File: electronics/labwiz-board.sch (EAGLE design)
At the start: 99 parts, among them J1 SD_MICRO_SDIO_1BIT, J2 CORTEX_DEBUGSMD_original, J3 DNP, U1 STM32F10XRXT6, U2 MCP73831/2, U4 MIC5219-3.3V, X2 M12_BOTTOM_CONTACTS_FPC_1MM, Y3 32.768kHz

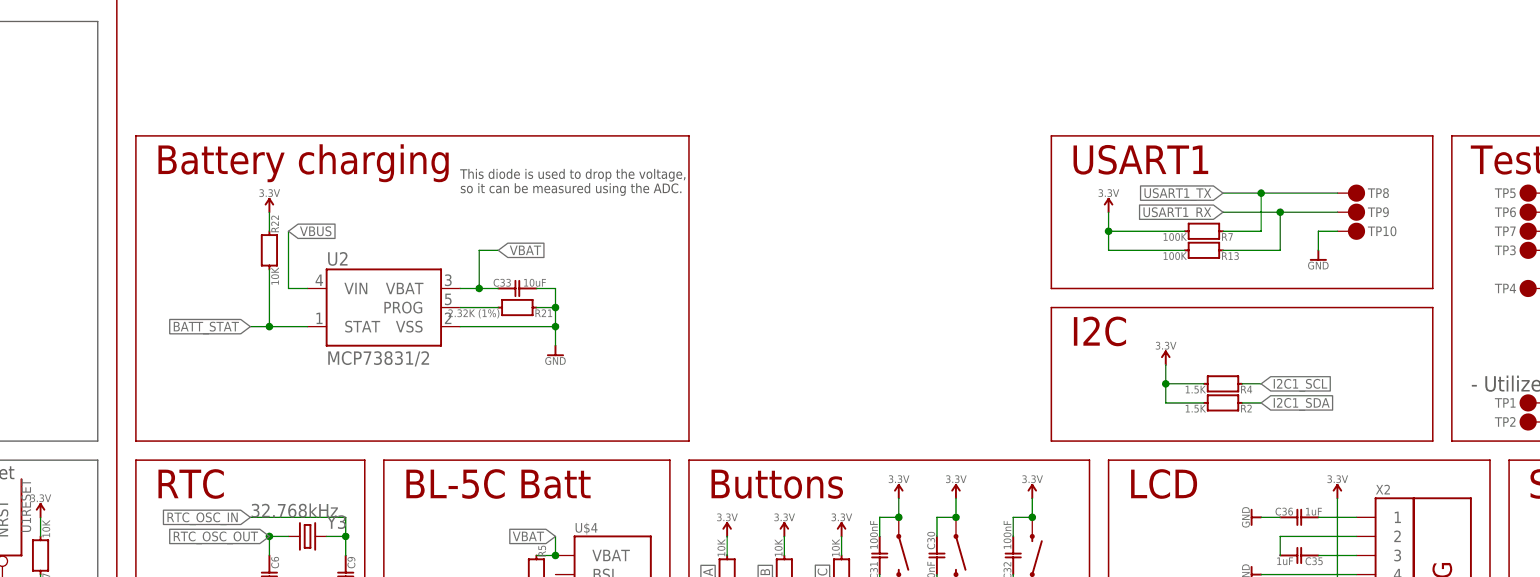
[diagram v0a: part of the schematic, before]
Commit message: Added 2x2 right angle header to board. Closes #105.
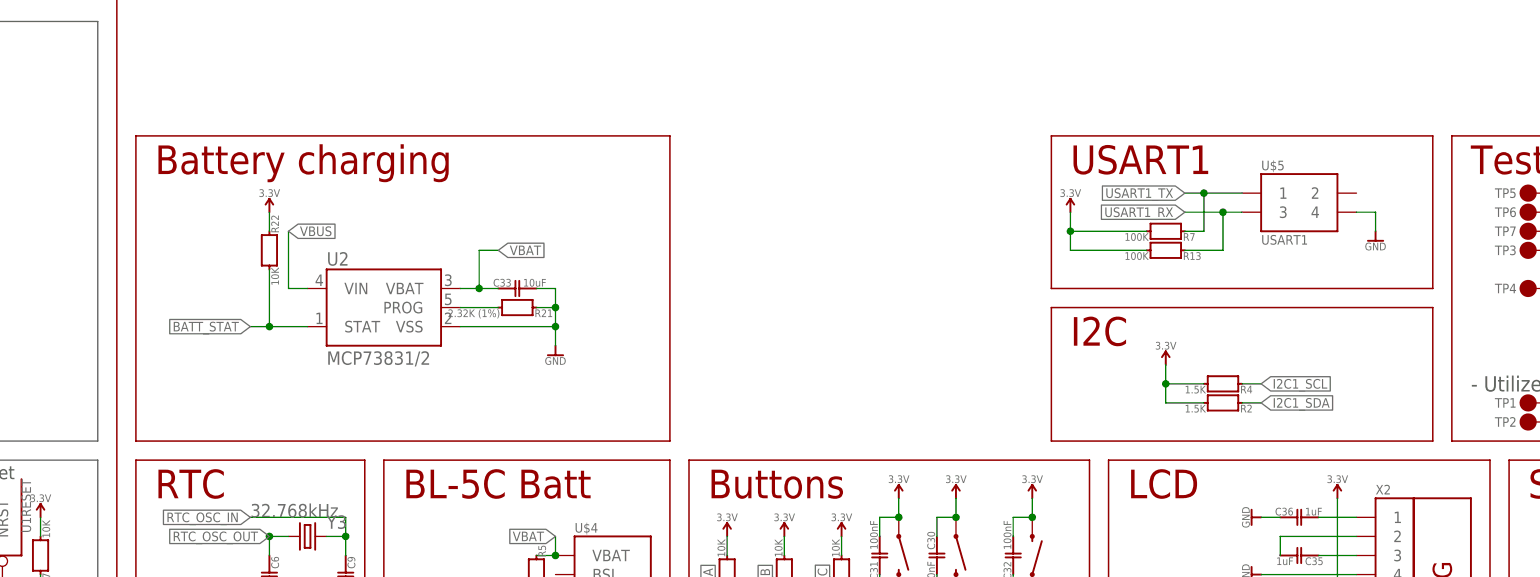
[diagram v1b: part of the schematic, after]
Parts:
- removed TP10, TP8, TP9: DNP, PaxInstruments-Connectors:M01_PAD_1MM
- added U$5: USART1, PaxInstruments-Connectors:M02X2_RIGHT_ANGLE
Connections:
- net GND: now also U$5.4; no longer TP10.P$1
- net USART1_RX: now also U$5.3; no longer TP9.P$1
- net USART1_TX: now also U$5.1; no longer TP8.P$1
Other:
- note removed: "This diode is used to drop the voltage, so it can be measured using the ADC."
- moved on the sheet: R13, R7
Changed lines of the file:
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@@
 <part name="TP7" library="PaxInstruments-Connectors" deviceset="M01" device="_PAD_1MM" value="DNP"/>
 <part name="GND21" library="PaxInstruments-Aesthetics" deviceset="GND" device="" value="GND"/>
-<part name="TP8" library="PaxInstruments-Connectors" deviceset="M01" device="_PAD_1MM" value="DNP"/>
-<part name="TP9" library="PaxInstruments-Connectors" deviceset="M01" device="_PAD_1MM" value="DNP"/>
-<part name="TP10" library="PaxInstruments-Connectors" deviceset="M01" device="_PAD_1MM" value="DNP"/>
 <part name="F1" library="PaxInstruments-RCL" deviceset="FUSE_RESETTABLE_PTC" device="_0805" technology="_1000MA" value="1000mA"/>
 <part name="Z3" library="PaxInstrument-T400" deviceset="SPARKFUN-RESISTORS_RESISTOR" device="0603-RES" value="PGB1010603">
@@
 <part name="C17" library="PaxInstruments-RCL" deviceset="CAPACITOR_FIXED" device="_0402" technology="_1UF" value="1uF"/>
 <part name="JP2" library="SparkFun-Jumpers" deviceset="JUMPER-SMT_3_1-NC_TRACE" device="_SILK"/>
+<part name="U$5" library="PaxInstruments-Connectors" deviceset="M02X2" device="_RIGHT_ANGLE" value="USART1"/>
 </parts>
 <sheets>
@@
 <wire x1="114.3" y1="5.08" x2="162.56" y2="5.08" width="0.2032" layer="94"/>
 <text x="116.84" y="40.64" size="3.81" layer="94">WiFi Module</text>
-<wire x1="187.96" y1="91.44" x2="187.96" y2="132.08" width="0.2032" layer="94"/>
-<wire x1="114.3" y1="132.08" x2="187.96" y2="132.08" width="0.2032" layer="94"/>
-<wire x1="114.3" y1="91.44" x2="187.96" y2="91.44" width="0.2032" layer="94"/>
+<wire x1="185.42" y1="91.44" x2="185.42" y2="132.08" width="0.2032" layer="94"/>
+<wire x1="114.3" y1="132.08" x2="185.42" y2="132.08" width="0.2032" layer="94"/>
+<wire x1="114.3" y1="91.44" x2="185.42" y2="91.44" width="0.2032" layer="94"/>
 <wire x1="114.3" y1="91.44" x2="114.3" y2="132.08" width="0.2032" layer="94"/>
 <text x="116.84" y="127" size="3.81" layer="94">Battery charging</text>
@@
 <wire x1="314.96" y1="198.12" x2="383.54" y2="198.12" width="0.2032" layer="94"/>
 <wire x1="383.54" y1="198.12" x2="383.54" y2="256.54" width="0.2032" layer="94"/>
-<text x="157.48" y="124.46" size="1.27" layer="97">This diode is used to drop the voltage,
-so it can be measured using the ADC.</text>
 <text x="93.98" y="185.42" size="1.27" layer="97">Shotkey diode</text>
 <text x="292.1" y="99.06" size="2.032" layer="97" align="center-left">- Utilize unused pins</text>
@@
 <instance part="C16" gate="G$1" x="165.1" y="63.5" rot="MR180"/>
 <instance part="TP7" gate="G$1" x="299.72" y="119.38" rot="R180"/>
-<instance part="GND21" gate="G$1" x="271.78" y="116.84"/>
-<instance part="TP8" gate="G$1" x="276.86" y="124.46"/>
-<instance part="TP9" gate="G$1" x="276.86" y="121.92"/>
-<instance part="TP10" gate="G$1" x="276.86" y="119.38"/>
+<instance part="GND21" gate="G$1" x="279.4" y="119.38"/>
 <instance part="F1" gate="G$1" x="45.72" y="185.42" rot="MR270"/>
 <instance part="Z3" gate="G$1" x="38.1" y="167.64" smashed="yes" rot="R90">
@@
 <attribute name="MF" x="38.1" y="167.64" size="1.778" layer="96" rot="R90" display="off"/>
 </instance>
-<instance part="R7" gate="G$1" x="256.54" y="119.38" rot="R90"/>
-<instance part="R13" gate="G$1" x="256.54" y="116.84" rot="R90"/>
-<instance part="SUPPLY5" gate="G$1" x="243.84" y="121.92"/>
+<instance part="R7" gate="G$1" x="251.46" y="119.38" rot="R90"/>
+<instance part="R13" gate="G$1" x="251.46" y="116.84" rot="R90"/>
+<instance part="SUPPLY5" gate="G$1" x="238.76" y="121.92"/>
 <instance part="C17" gate="G$1" x="83.82" y="66.04"/>
 <instance part="JP2" gate="G$1" x="53.34" y="170.18" smashed="yes" rot="MR0">
 <attribute name="NAME" x="58.42" y="173.101" size="1.778" layer="95" font="vector" rot="MR0"/>
 </instance>
+<instance part="U$5" gate="G$1" x="269.24" y="121.92"/>
 </instances>
 <busses>
@@
 <pinref part="R13" gate="G$1" pin="1"/>
 <pinref part="SUPPLY5" gate="G$1" pin="3.3V"/>
-<wire x1="254" y1="116.84" x2="243.84" y2="116.84" width="0.1524" layer="91"/>
-<wire x1="243.84" y1="116.84" x2="243.84" y2="119.38" width="0.1524" layer="91"/>
+<wire x1="248.92" y1="116.84" x2="238.76" y2="116.84" width="0.1524" layer="91"/>
+<wire x1="238.76" y1="116.84" x2="238.76" y2="119.38" width="0.1524" layer="91"/>
 <pinref part="R7" gate="G$1" pin="1"/>
-<wire x1="243.84" y1="119.38" x2="243.84" y2="121.92" width="0.1524" layer="91"/>
-<wire x1="254" y1="119.38" x2="243.84" y2="119.38" width="0.1524" layer="91"/>
-<junction x="243.84" y="119.38"/>
+<wire x1="238.76" y1="119.38" x2="238.76" y2="121.92" width="0.1524" layer="91"/>
+<wire x1="248.92" y1="119.38" x2="238.76" y2="119.38" width="0.1524" layer="91"/>
+<junction x="238.76" y="119.38"/>
 </segment>
 <segment>
@@
 </segment>
 <segment>
-<pinref part="GND21" gate="G$1" pin="GND"/>
-<wire x1="274.32" y1="119.38" x2="271.78" y2="119.38" width="0.1524" layer="91"/>
-<wire x1="271.78" y1="119.38" x2="271.78" y2="116.84" width="0.1524" layer="91"/>
-<pinref part="TP10" gate="G$1" pin="P$1"/>
-</segment>
-<segment>
 <pinref part="R16" gate="G$1" pin="1"/>
 <pinref part="GND33" gate="G$1" pin="GND"/>
 <wire x1="223.52" y1="60.96" x2="223.52" y2="53.34" width="0.1524" layer="91"/>
+</segment>
+<segment>
+<pinref part="U$5" gate="G$1" pin="4"/>
+<pinref part="GND21" gate="G$1" pin="GND"/>
+<wire x1="276.86" y1="121.92" x2="279.4" y2="121.92" width="0.1524" layer="91"/>
+<wire x1="279.4" y1="121.92" x2="279.4" y2="119.38" width="0.1524" layer="91"/>
 </segment>
 </net>
@@
 </segment>
 <segment>
-<label x="259.08" y="124.46" size="1.27" layer="95" rot="R180" xref="yes"/>
-<wire x1="259.08" y1="124.46" x2="264.16" y2="124.46" width="0.1524" layer="91"/>
-<pinref part="TP8" gate="G$1" pin="P$1"/>
+<label x="254" y="124.46" size="1.27" layer="95" rot="R180" xref="yes"/>
+<wire x1="254" y1="124.46" x2="256.54" y2="124.46" width="0.1524" layer="91"/>
 <pinref part="R7" gate="G$1" pin="2"/>
-<wire x1="264.16" y1="124.46" x2="274.32" y2="124.46" width="0.1524" layer="91"/>
-<wire x1="259.08" y1="119.38" x2="264.16" y2="119.38" width="0.1524" layer="91"/>
-<wire x1="264.16" y1="119.38" x2="264.16" y2="124.46" width="0.1524" layer="91"/>
-<junction x="264.16" y="124.46"/>
+<wire x1="254" y1="119.38" x2="256.54" y2="119.38" width="0.1524" layer="91"/>
+<wire x1="256.54" y1="119.38" x2="256.54" y2="124.46" width="0.1524" layer="91"/>
+<junction x="256.54" y="124.46"/>
+<pinref part="U$5" gate="G$1" pin="1"/>
+<wire x1="256.54" y1="124.46" x2="261.62" y2="124.46" width="0.1524" layer="91"/>
 </segment>
 <segment>
@@
 </segment>
 <segment>
-<label x="259.08" y="121.92" size="1.27" layer="95" rot="R180" xref="yes"/>
-<wire x1="259.08" y1="121.92" x2="266.7" y2="121.92" width="0.1524" layer="91"/>
-<pinref part="TP9" gate="G$1" pin="P$1"/>
+<label x="254" y="121.92" size="1.27" layer="95" rot="R180" xref="yes"/>
+<wire x1="254" y1="121.92" x2="259.08" y2="121.92" width="0.1524" layer="91"/>
 <pinref part="R13" gate="G$1" pin="2"/>
-<wire x1="266.7" y1="121.92" x2="274.32" y2="121.92" width="0.1524" layer="91"/>
-<wire x1="259.08" y1="116.84" x2="266.7" y2="116.84" width="0.1524" layer="91"/>
-<wire x1="266.7" y1="116.84" x2="266.7" y2="121.92" width="0.1524" layer="91"/>
-<junction x="266.7" y="121.92"/>
-</segment>
-<segment>
+<wire x1="254" y1="116.84" x2="259.08" y2="116.84" width="0.1524" layer="91"/>
+<wire x1="259.08" y1="116.84" x2="259.08" y2="121.92" width="0.1524" layer="91"/>
+<junction x="259.08" y="121.92"/>
+<pinref part="U$5" gate="G$1" pin="3"/>
+<wire x1="259.08" y1="121.92" x2="261.62" y2="121.92" width="0.1524" layer="91"/>
+</segment>
+<segment>

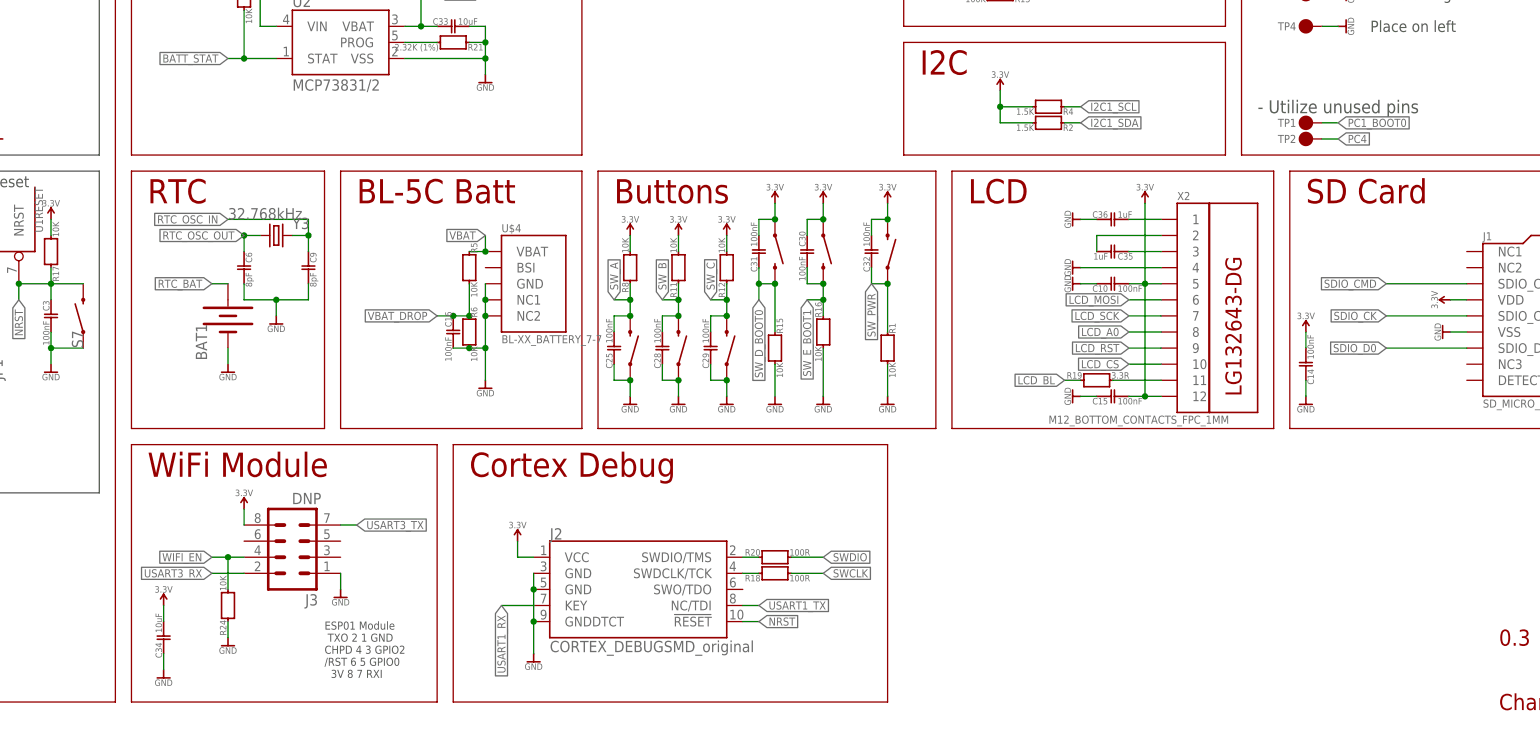
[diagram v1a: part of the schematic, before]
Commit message: Moved to ESP-09 WiFi modules. Still some work to be done.
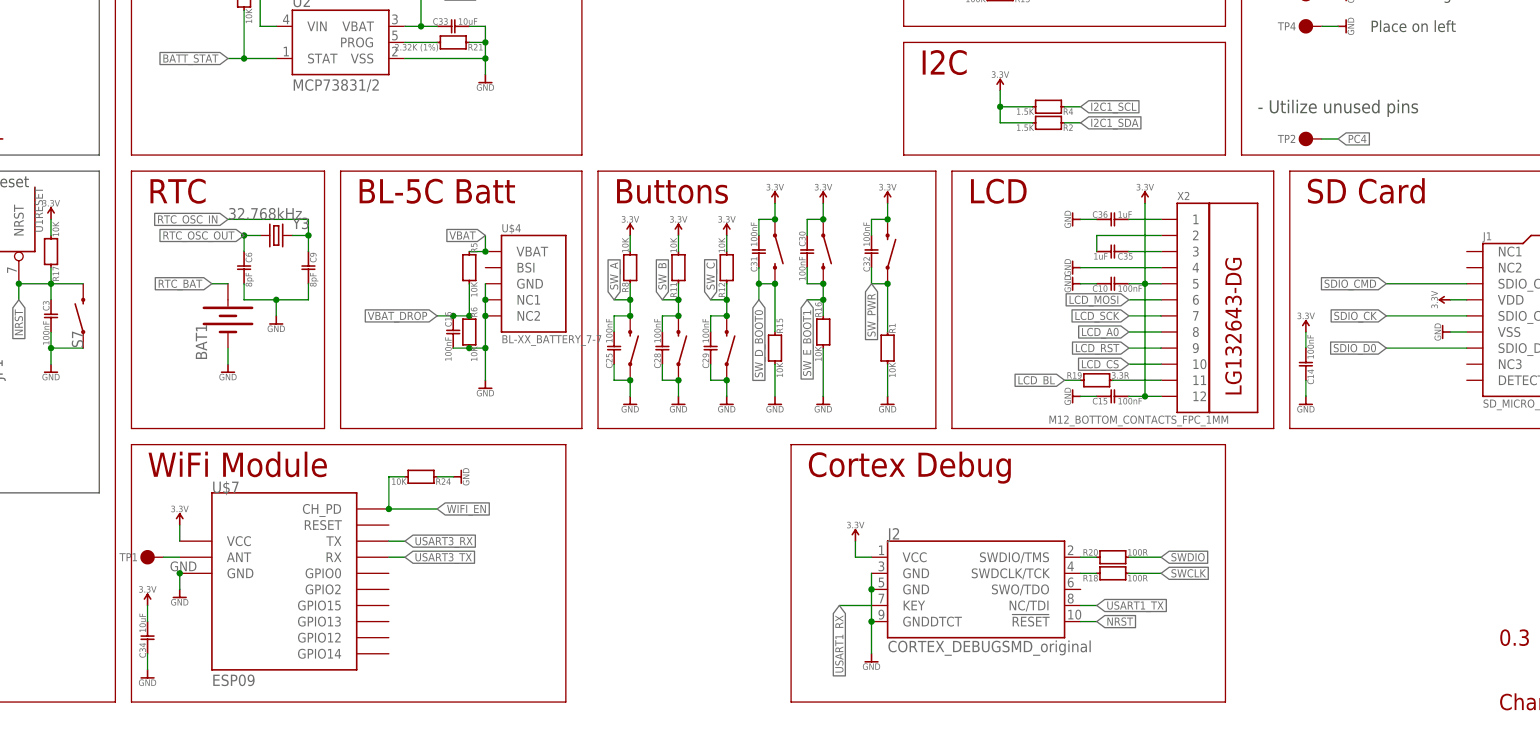
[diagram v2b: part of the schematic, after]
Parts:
- removed J3: DNP, SparkFun-Connectors:M04X2
- added U$7: ESP09, PaxInstruments-DigitalIC:ESP09
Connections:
- new net N$13: TP1.P$1, U$7.ANT
- net 3.3V: now also U$7.VCC; no longer J3.8
- net GND: now also U$7.GND, U$7.GND1, U$7.GND2, U$7.GND3, U$7.GND4, U$7.GND5, U$7.GND6, U$7.GND7; no longer J3.1
- net PC1_BOOT0: no longer TP1.P$1
- net USART3_RX: now also U$7.TX; no longer J3.2
- net USART3_TX: now also U$7.RX; no longer J3.7
- net WIFI_EN: now also U$7.CH_PD; no longer J3.4
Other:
- note removed: "ESP01 Module TXO 2 1 GND CHPD 4 3 GPIO2 /RST 6 5 GPIO0 3V 8 7 RXI"
- moved on the sheet: C34, J2, R18, R20, R24, TP1

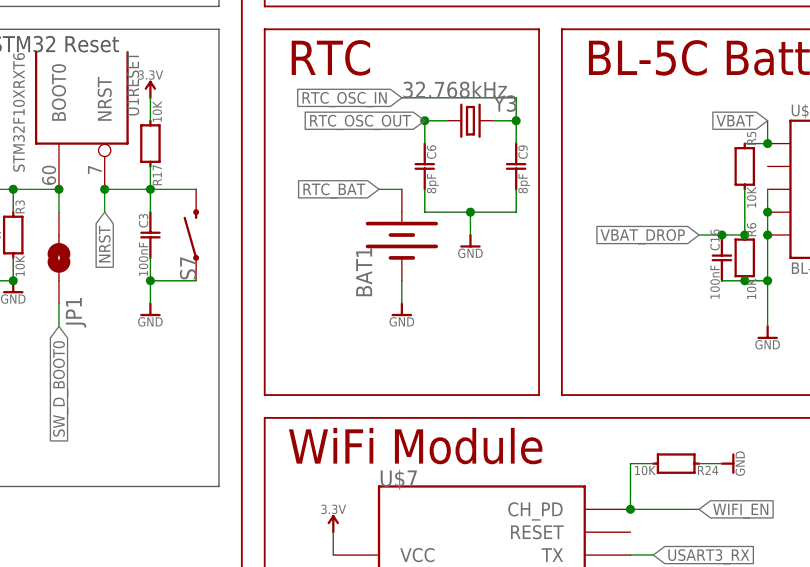
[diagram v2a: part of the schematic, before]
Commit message: Added pin interrupt info to a page on the pin-map spreadsheet. Changed RTC battery to a CR1025. CR1025 connections still need to be routed.
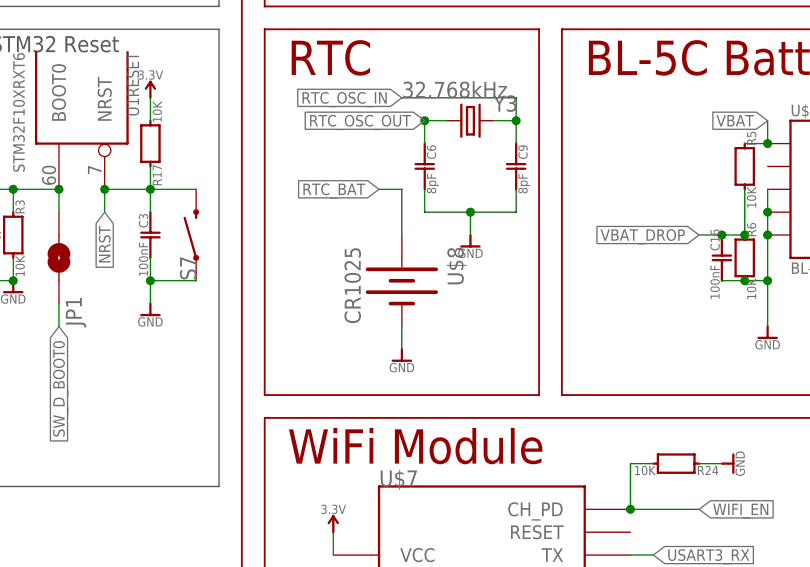
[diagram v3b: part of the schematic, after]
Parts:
- removed BAT1: (no value), PaxInstruments-Electromechanical:BATTERY12MM
- added U$8: CR1025, PaxInstruments-Electromechanical:CR1025
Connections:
- net GND: now also U$8.-; no longer BAT1.-
- net RTC_BAT: now also U$8.+; no longer BAT1.+
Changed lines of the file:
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@@
 <part name="C9" library="PaxInstruments-RCL" deviceset="CAPACITOR_FIXED" device="_0402" technology="_8PF" value="8pF"/>
 <part name="GND5" library="PaxInstruments-Aesthetics" deviceset="GND" device="" value="GND"/>
-<part name="BAT1" library="PaxInstruments-Electromechanical" deviceset="BATTERY" device="12MM"/>
 <part name="U$2" library="SparkFun-Aesthetics" deviceset="FOUR_LAYER_WARNING" device="" value="DNP"/>
 <part name="R18" library="PaxInstruments-RCL" deviceset="RESISTOR_FIXED" device="_0402" technology="_100R" value="100R"/>
@@
 <part name="SUPPLY10" library="PaxInstruments-Aesthetics" deviceset="SYM_VCC" device="" technology="3.3V" value="3.3V"/>
 <part name="TP1" library="PaxInstruments-Connectors" deviceset="M01" device="_PAD_1MM" value="DNP"/>
+<part name="U$8" library="PaxInstruments-Electromechanical" deviceset="CR1025" device=""/>
 </parts>
 <sheets>
@@
 <instance part="C6" gate="G$1" x="132.08" y="73.66" rot="R180"/>
 <instance part="C9" gate="G$1" x="142.24" y="73.66" rot="R180"/>
-<instance part="GND5" gate="G$1" x="129.54" y="58.42"/>
-<instance part="BAT1" gate="G$1" x="129.54" y="66.04" smashed="yes" rot="R270">
-<attribute name="NAME" x="124.46" y="64.77" size="1.778" layer="95" rot="R270"/>
-<attribute name="VALUE" x="123.19" y="69.85" size="1.778" layer="96" rot="R270"/>
-</instance>
+<instance part="GND5" gate="G$1" x="129.54" y="53.34"/>
 <instance part="U$2" gate="G$1" x="342.9" y="15.24"/>
 <instance part="R18" gate="G$1" x="269.24" y="25.4" rot="MR90"/>
@@
 <instance part="SUPPLY10" gate="G$1" x="121.92" y="33.02"/>
 <instance part="TP1" gate="G$1" x="116.84" y="27.94" rot="R180"/>
+<instance part="U$8" gate="G$1" x="129.54" y="60.96" rot="R270"/>
 </instances>
 <busses>
@@
 </segment>
 <segment>
-<pinref part="BAT1" gate="G$1" pin="-"/>
 <pinref part="GND5" gate="G$1" pin="GND"/>
-<wire x1="129.54" y1="60.96" x2="129.54" y2="58.42" width="0.1524" layer="91"/>
+<pinref part="U$8" gate="G$1" pin="-"/>
+<wire x1="129.54" y1="53.34" x2="129.54" y2="55.88" width="0.1524" layer="91"/>
 </segment>
 <segment>
@@
 </segment>
 <segment>
+<wire x1="129.54" y1="66.04" x2="129.54" y2="71.12" width="0.1524" layer="91"/>
 <wire x1="129.54" y1="71.12" x2="127" y2="71.12" width="0.1524" layer="91"/>
-<pinref part="BAT1" gate="G$1" pin="+"/>
-</segment>
-</net>
+<pinref part="U$8" gate="G$1" pin="+"/>
+</segment>
+</net>
